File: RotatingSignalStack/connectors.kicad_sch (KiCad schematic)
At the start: 5 parts, among them J4 Conn_ARM_JTAG_SWD_20

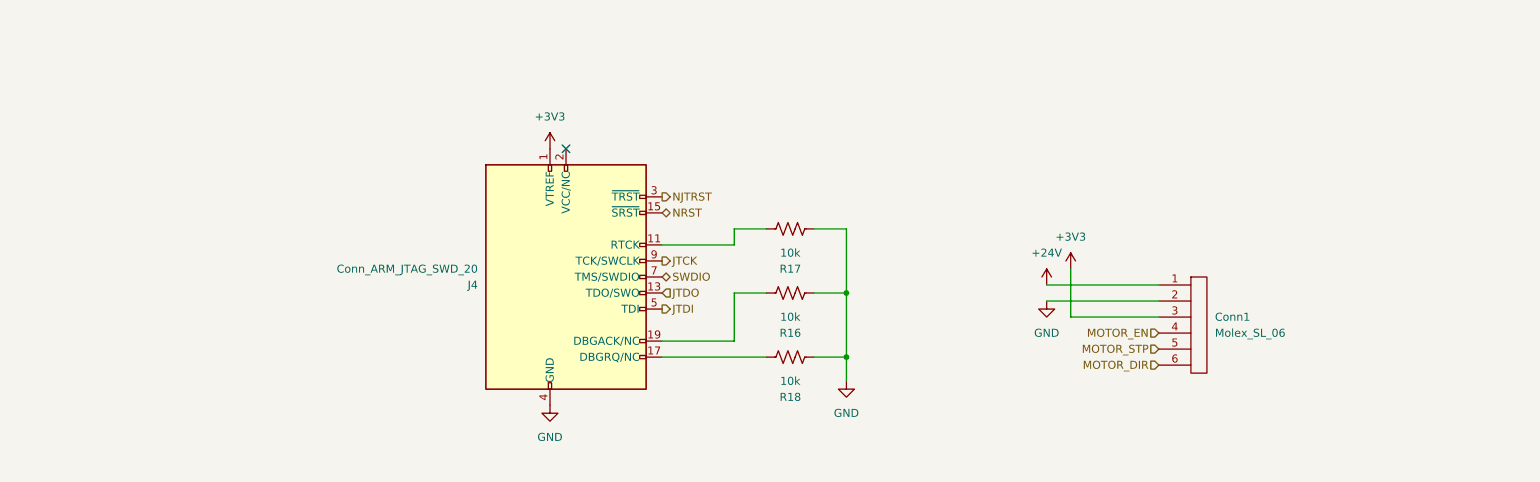
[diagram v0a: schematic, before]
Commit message: Added Compass ESD protection
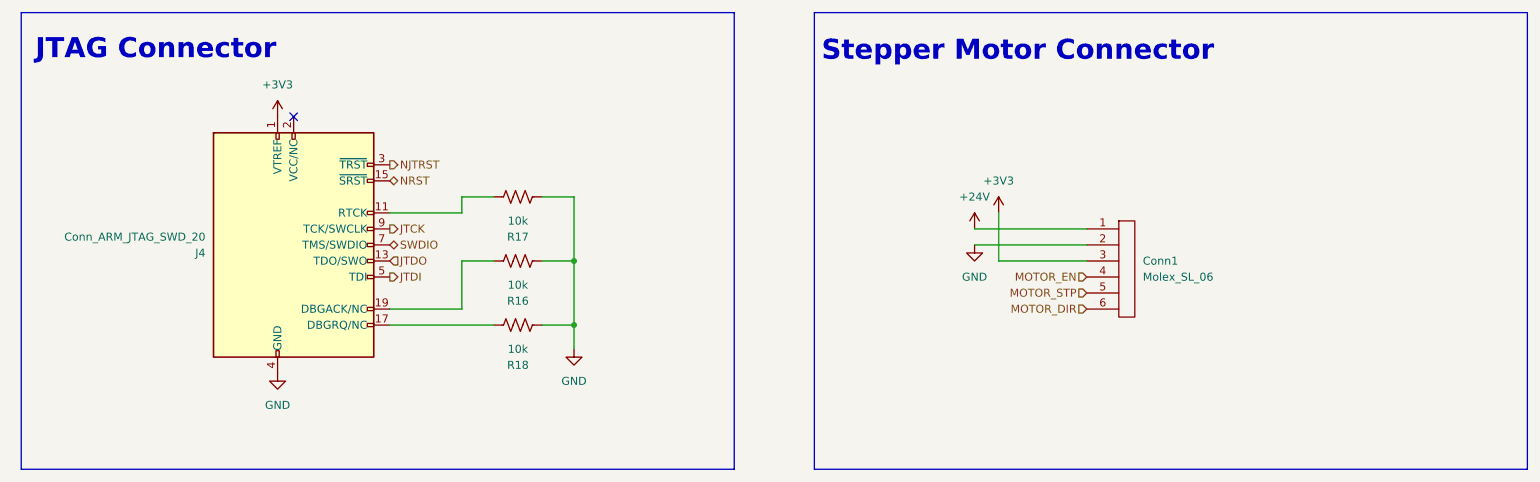
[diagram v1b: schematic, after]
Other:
- note added: "JTAG Connector"
- note added: "Stepper Motor Connector"
- moved on the sheet: Conn1, J4, R16, R17, R18

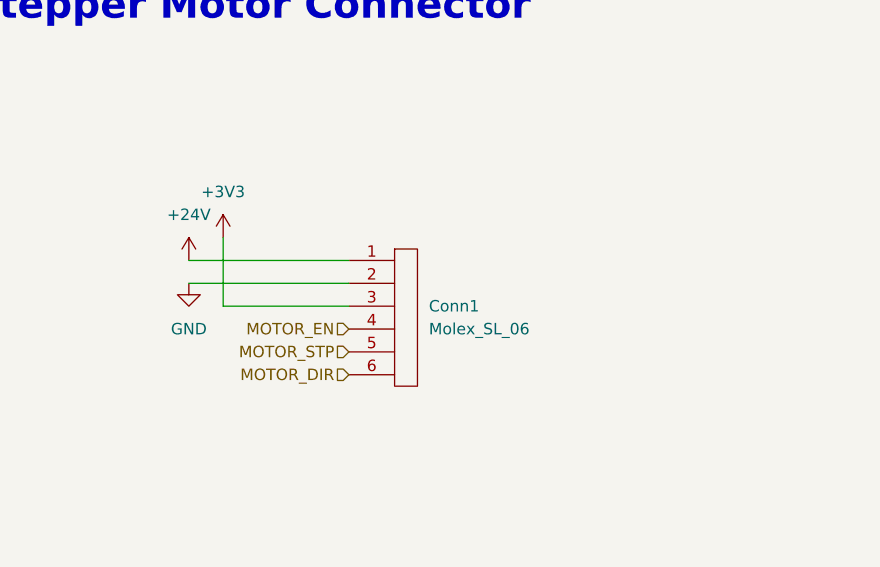
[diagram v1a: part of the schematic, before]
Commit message: Added Motor connector CAN
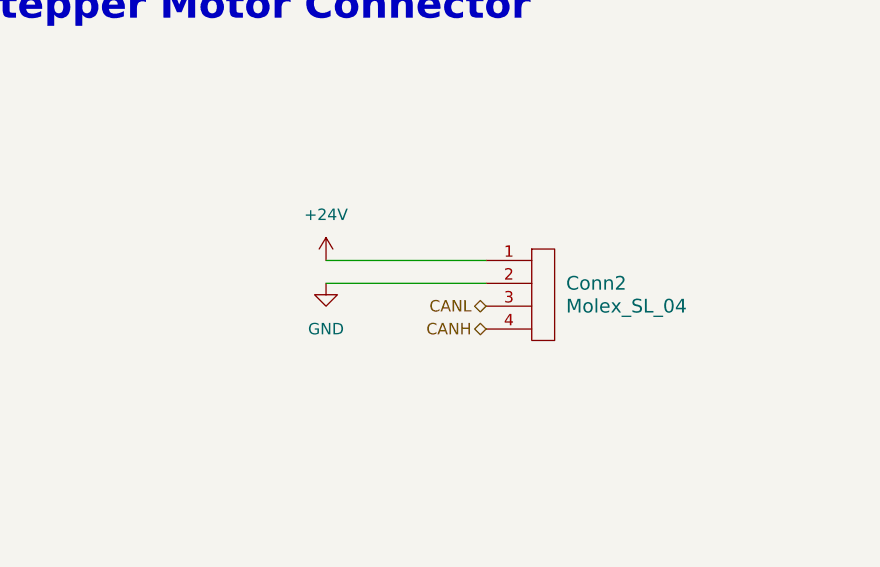
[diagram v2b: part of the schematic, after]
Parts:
- removed Conn1: Molex_SL_06, symbol MRDT_Connectors:Molex_SL_06
- added Conn2: Molex_SL_04, symbol MRDT_Connectors:Molex_SL_04
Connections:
- net +24V: now also Conn2.1
- net GND: now also Conn2.2
- new net CANH: Conn2.4
- new net CANL: Conn2.3

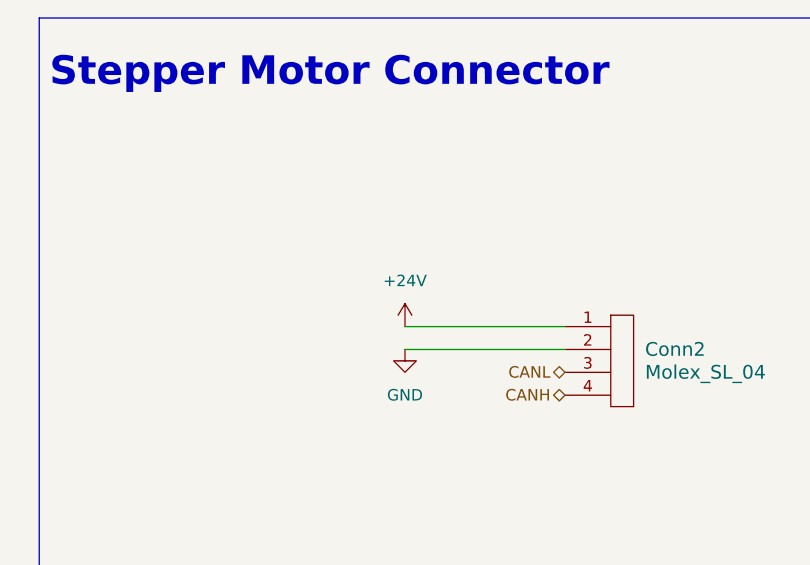
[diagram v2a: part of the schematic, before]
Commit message: Added power LEDS
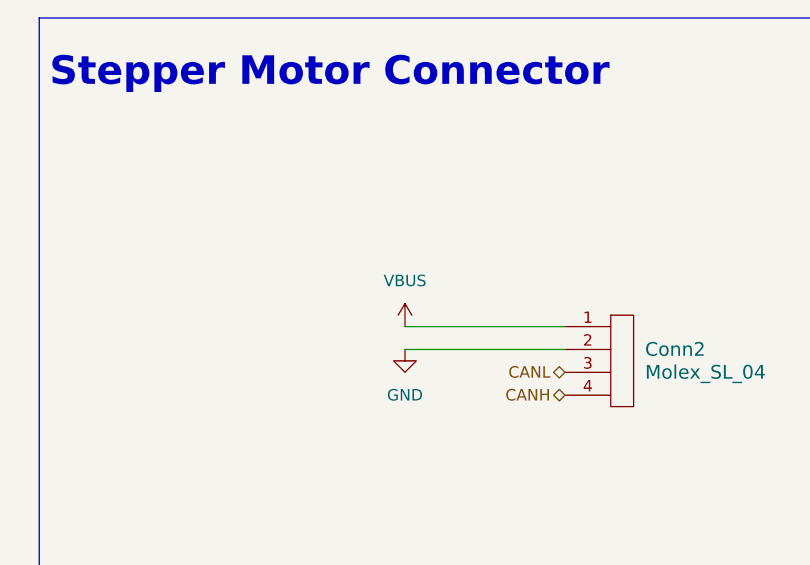
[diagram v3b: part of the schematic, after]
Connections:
- net +24V renamed VBUS
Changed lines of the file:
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@@
 	)
 	(symbol
-		(lib_id "power:+24V")
+		(lib_id "power:VBUS")
 		(at 187.96 55.88 0)
 		(unit 1)
@@
 		(dnp no)
 		(fields_autoplaced yes)
-		(property "Reference" "#PWR020"
+		(property "Reference" "#PWR049"
 			(at 187.96 59.69 0)
 			(effects
@@
 			)
 		)
-		(property "Value" "+24V"
+		(property "Value" "VBUS"
 			(at 187.96 50.8 0)
 			(effects
@@
 			)
 		)
-		(property "Description" "Power symbol creates a global label with name \"+24V\""
+		(property "Description" "Power symbol creates a global label with name \"VBUS\""
 			(at 187.96 55.88 0)
 			(effects
@@
 		)
 		(instances
-			(project "RotatingSignalStack"
+			(project ""
 				(path "/fbbbfa89-3c28-4cf8-856b-66ca7308742c/e54c0f4b-dfe7-45e5-9ea6-eafbeb6efeec"
-					(reference "#PWR020")
+					(reference "#PWR049")
 					(unit 1)
 				)

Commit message: Added everything
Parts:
- removed J4: Conn_ARM_JTAG_SWD_20, symbol Connector:Conn_ARM_JTAG_SWD_20
- removed R16, R17, R18: 10k, symbol Device:R_US
- added J2: Conn_ARM_SWD_TagConnect_TC2030-NL, Connector:Tag-Connect_TC2030-IDC-NL_2x03_P1.27mm_Vertical, symbol Connector:Conn_ARM_SWD_TagConnect_TC2030-NL
- Conn2: footprint (none) -> MRDT_Connectors:MOLEX_SL_04_Horizontal
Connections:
- net +3V3: now also J2.1 (VCC)
- net GND: now also J2.5 (GND)
- net NRST: now also J2.3 (~{RESET})
- net SWDIO: now also J2.2 (SWDIO)
- new net SWDCLK: J2.4 (SWCLK)
- new net SWO: J2.6 (SWO)
- no-connect marks 1 -> 0
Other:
- note added: "SWD Connector"
- note removed: "JTAG Connector"
